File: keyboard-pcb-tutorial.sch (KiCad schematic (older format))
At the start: 14 parts

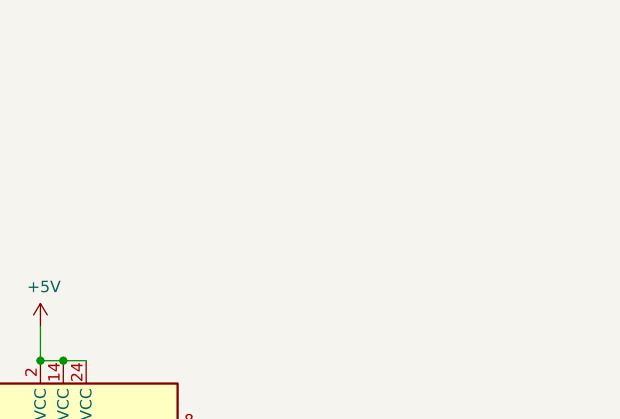
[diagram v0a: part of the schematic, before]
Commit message: add usb symbol
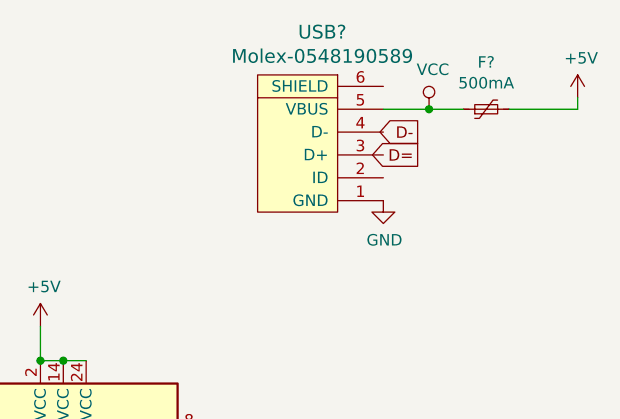
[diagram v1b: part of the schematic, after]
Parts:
- added F?: 500mA, symbol Device:Polyfuse_Small
- added USB?: Molex-0548190589, symbol random-keyboard-parts:Molex-0548190589
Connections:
- net +5V: now also F?.2
- net GND: now also USB?.1 (GND)
- new net VCC: F?.1, USB?.5 (VBUS)
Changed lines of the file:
@@
 Text GLabel 6900 3400 0    50   Input ~ 0
 D-
+$Comp
+L random-keyboard-parts:Molex-0548190589 USB?
+U 1 1 60F943EE
+P 9750 1100
+F 0 "USB?" V 10287 1067 60  0000 C CNN
+F 1 "Molex-0548190589" V 10181 1067 60  0000 C CNN
+F 2 "" H 9750 1100 60  0001 C CNN
+F 3 "" H 9750 1100 60  0001 C CNN
+	1    9750 1100
+	0    -1   -1   0
+$EndComp
+$Comp
+L Device:Polyfuse_Small F?
+U 1 1 60F94AA6
+P 10500 900
+F 0 "F?" V 10705 900 50  0000 C CNN
+F 1 "500mA" V 10614 900 50  0000 C CNN
+F 2 "" H 10550 700 50  0001 L CNN
+F 3 "~" H 10500 900 50  0001 C CNN
+	1    10500 900
+	0    -1   -1   0
+$EndComp
+Wire Wire Line
+	10600 900  10900 900
+Wire Wire Line
+	10900 900  10900 850
+$Comp
+L power:+5V #PWR?
+U 1 1 60F98656
+P 10900 850
+F 0 "#PWR?" H 10900 700 50  0001 C CNN
+F 1 "+5V" H 10915 1023 50  0000 C CNN
+F 2 "" H 10900 850 50  0001 C CNN
+F 3 "" H 10900 850 50  0001 C CNN
+	1    10900 850
+	1    0    0    -1
+$EndComp
+Wire Wire Line
+	10400 900  10250 900
+$Comp
+L power:VCC #PWR?
+U 1 1 60F99C54
+P 10250 900
+F 0 "#PWR?" H 10250 750 50  0001 C CNN
+F 1 "VCC" H 10267 1073 50  0000 C CNN
+F 2 "" H 10250 900 50  0001 C CNN
+F 3 "" H 10250 900 50  0001 C CNN
+	1    10250 900
+	1    0    0    -1
+$EndComp
+Wire Wire Line
+	10250 900  10050 900
+Connection ~ 10250 900
+Text GLabel 10200 1000 0    50   Output ~ 0
+D-
+Text GLabel 10200 1100 0    50   Output ~ 0
+D=
+$Comp
+L power:GND #PWR?
+U 1 1 60F9CE3E
+P 10050 1300
+F 0 "#PWR?" H 10050 1050 50  0001 C CNN
+F 1 "GND" H 10055 1127 50  0000 C CNN
+F 2 "" H 10050 1300 50  0001 C CNN
+F 3 "" H 10050 1300 50  0001 C CNN
+	1    10050 1300
+	1    0    0    -1
+$EndComp
 $EndSCHEMATC

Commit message: update footprint
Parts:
- added D1, D2, D3, D4: D_Small, Diode_SMD:D_SOD-123, symbol Device:D_Small
- added MX1, MX2, MX3, MX4: MX-NoLED, symbol MX_Alps_Hybrid:MX-NoLED
- C1, C2, C3, C4, C5, C6, C7: renamed from C?; footprint (none) -> Capacitor_SMD:C_0805_2012Metric
- F1: renamed from F?; footprint (none) -> Fuse:Fuse_1206_3216Metric
- R1, R2, R3, R4: renamed from R?; footprint (none) -> Resistor_SMD:R_0805_2012Metric
- USB1: renamed from USB?; footprint (none) -> random-keyboard-parts:SKQG-1155865
- Y1: renamed from Y?; footprint (none) -> Crystal:Crystal_SMD_3225-4Pin_3.2x2.5mm
- gave numbers to parts that had none: 2
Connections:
- net labels added: COL0, COL1, ROW0, ROW1
- wire segments 44 -> 56
